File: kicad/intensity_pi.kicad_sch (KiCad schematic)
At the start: 68 parts, among them J1 Input A, J2 Input B / Setpoint, J3 Monitor, J4 Output, J7 select 1, SW1 SW_SPDT, SW2 SW_SPDT, SW3 SW_SPDT, SW5 EG6100-ND, U1 LM4040DBZ-5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

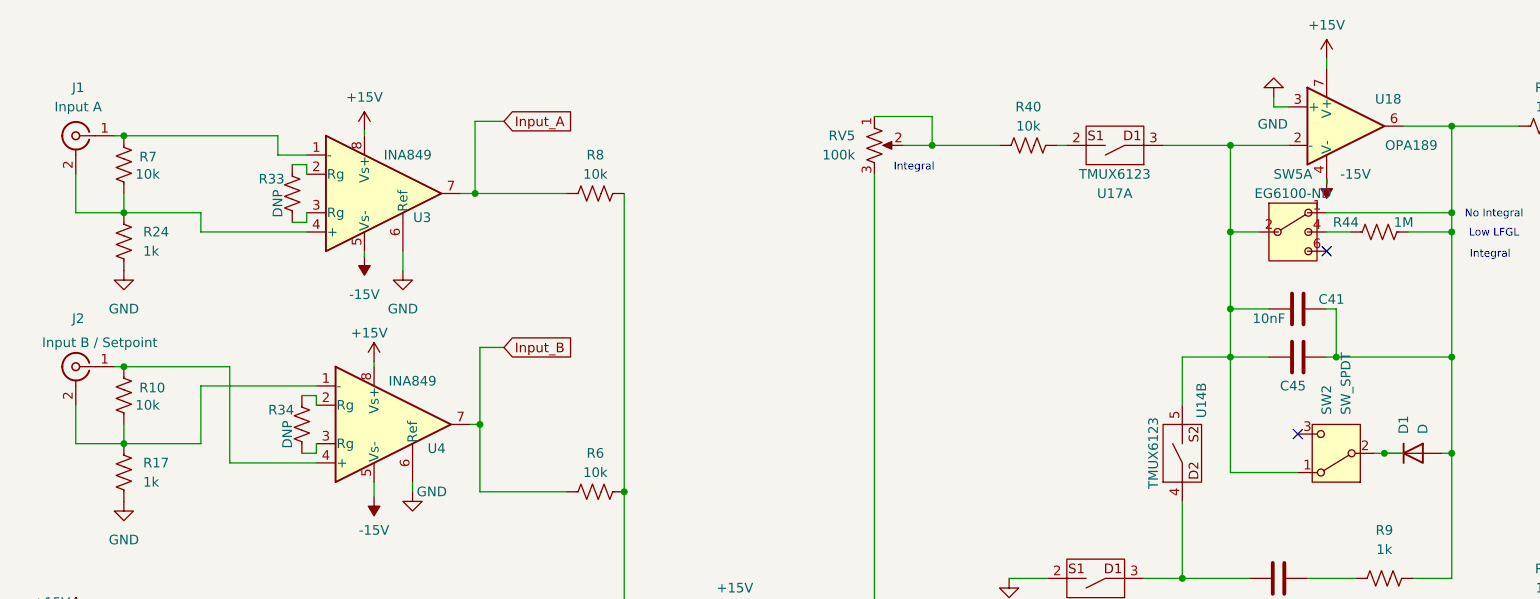
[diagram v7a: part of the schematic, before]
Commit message: V1.1, Fixedincorrect footprints for Green/Red LED, Diodes, Mosfets, Flipped Input A/B Polarity, Potentiometer labels, Incorrect part nos for V regulators. No functionality changes
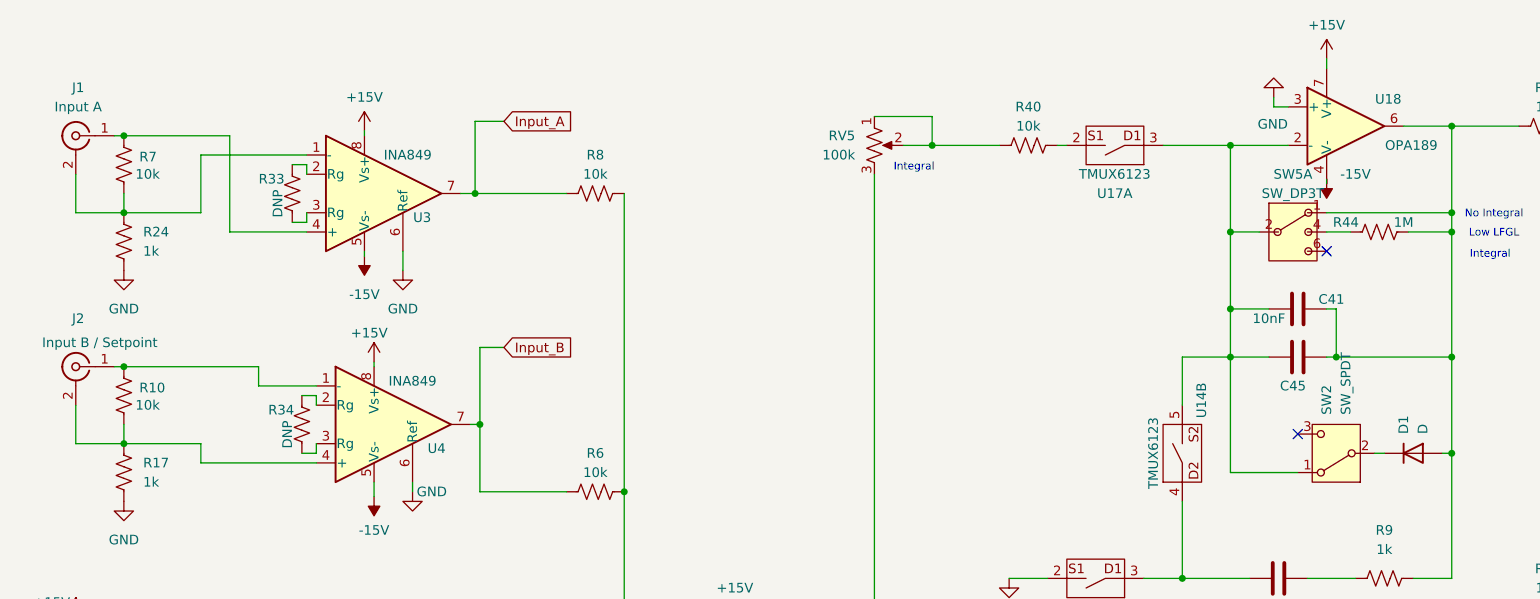
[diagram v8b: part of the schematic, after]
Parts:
- SW5: value EG6100-ND -> SW_DP3T
- U3, U4: PARTNO INA849DR‎ -> INA849DR
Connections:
- net at J1.1 (In), R7.2: now also U3.4 (+); no longer U3.1 (-)
- net at J1.2 (Ext), R24.2, R7.1: now also U3.1 (-); no longer U3.4 (+)
- net at C41.1, C45.2, R19.1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: now also D1.3 (A); no longer D1.2 (A)
- net at J2.2 (Ext), R10.1, R17.2: now also U4.4 (+); no longer U4.1 (-)
- net at J2.1 (In), R10.2: now also U4.1 (-); no longer U4.4 (+)
- net at SW3.2 (B): now also D2.3 (A); no longer D2.2 (A)
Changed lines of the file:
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@@
 	)
 	(junction
-		(at 191.77 71.12)
+		(at 25.4 29.21)
 		(diameter 0)
 		(color 0 0 0 0)
@@
 	)
 	(junction
-		(at 25.4 29.21)
-		(diameter 0)
-		(color 0 0 0 0)
-	)
-	(junction
 		(at 200.66 58.42)
 		(diameter 0)
@@
 	(wire
 		(pts
+			(xy 25.4 29.21) (xy 39.37 29.21)
+		)
+		(stroke
+			(width 0)
+			(type default)
+		)
+	)
+	(wire
+		(pts
 			(xy 219.71 91.44) (xy 219.71 104.14)
 		)
@@
 	(wire
 		(pts
+			(xy 35.56 39.37) (xy 35.56 31.75)
+		)
+		(stroke
+			(width 0)
+			(type default)
+		)
+	)
+	(wire
+		(pts
 			(xy 72.39 144.78) (xy 72.39 135.89)
 		)
@@
 	(wire
 		(pts
-			(xy 191.77 71.12) (xy 194.31 71.12)
-		)
-		(stroke
-			(width 0)
-			(type default)
-		)
-	)
-	(wire
-		(pts
 			(xy 59.69 173.99) (xy 59.69 177.8)
 		)
@@
 	(wire
 		(pts
-			(xy 158.75 181.61) (xy 157.48 181.61)
+			(xy 43.18 59.69) (xy 43.18 62.23)
 		)
 		(stroke
@@
 	(wire
 		(pts
-			(xy 165.1 58.42) (xy 171.45 58.42)
+			(xy 158.75 181.61) (xy 157.48 181.61)
 		)
 		(stroke
@@
 	(wire
 		(pts
-			(xy 106.045 93.345) (xy 106.045 93.98)
+			(xy 165.1 58.42) (xy 171.45 58.42)
 		)
 		(stroke
@@
 	(wire
 		(pts
-			(xy 34.29 116.84) (xy 37.465 116.84)
+			(xy 106.045 93.345) (xy 106.045 93.98)
 		)
 		(stroke
@@
 	(wire
 		(pts
-			(xy 189.23 135.89) (xy 203.2 135.89)
+			(xy 34.29 116.84) (xy 37.465 116.84)
 		)
 		(stroke
@@
 	(wire
 		(pts
-			(xy 35.56 41.91) (xy 49.53 41.91)
+			(xy 189.23 135.89) (xy 203.2 135.89)
 		)
 		(stroke
@@
 	(wire
 		(pts
-			(xy 35.56 41.91) (xy 35.56 39.37)
-		)
-		(stroke
-			(width 0)
-			(type default)
-		)
-	)
-	(wire
-		(pts
 			(xy 147.32 128.27) (xy 147.32 130.81)
 		)
@@
 	(wire
 		(pts
-			(xy 118.11 121.92) (xy 118.11 123.19)
+			(xy 39.37 29.21) (xy 39.37 41.91)
 		)
 		(stroke
@@
 	(wire
 		(pts
-			(xy 52.07 135.89) (xy 52.07 138.43)
+			(xy 118.11 121.92) (xy 118.11 123.19)
 		)
 		(stroke
@@
 	(wire
 		(pts
-			(xy 184.15 58.42) (xy 185.42 58.42)
+			(xy 52.07 135.89) (xy 52.07 138.43)
 		)
 		(stroke
@@
 	(wire
 		(pts
-			(xy 45.72 29.21) (xy 45.72 31.75)
+			(xy 184.15 58.42) (xy 185.42 58.42)
 		)
 		(stroke
@@
 	(wire
 		(pts
+			(xy 35.56 31.75) (xy 49.53 31.75)
+		)
+		(stroke
+			(width 0)
+			(type default)
+		)
+	)
+	(wire
+		(pts
 			(xy 72.39 119.38) (xy 72.39 135.89)
 		)
@@
 	(wire
 		(pts
-			(xy 35.56 62.23) (xy 50.8 62.23)
-		)
-		(stroke
-			(width 0)
-			(type default)
-		)
-	)
-	(wire
-		(pts
 			(xy 22.86 130.81) (xy 19.05 130.81)
 		)
@@
 	(wire
 		(pts
-			(xy 39.37 72.39) (xy 50.8 72.39)
-		)
-		(stroke
-			(width 0)
-			(type default)
-		)
-	)
-	(wire
-		(pts
 			(xy 203.2 151.765) (xy 203.2 160.02)
 		)
@@
 	(wire
 		(pts
-			(xy 116.84 196.85) (xy 116.84 184.15)
+			(xy 35.56 69.85) (xy 35.56 72.39)
 		)
 		(stroke
@@
 	(wire
 		(pts
-			(xy 25.4 29.21) (xy 45.72 29.21)
+			(xy 116.84 196.85) (xy 116.84 184.15)
 		)
 		(stroke
@@
 	(wire
 		(pts
-			(xy 132.08 26.67) (xy 132.08 30.48)
+			(xy 39.37 41.91) (xy 49.53 41.91)
 		)
 		(stroke
@@
 	(wire
 		(pts
-			(xy 219.71 114.3) (xy 234.315 114.3)
+			(xy 132.08 26.67) (xy 132.08 30.48)
 		)
 		(stroke
@@
 	(wire
 		(pts
-			(xy 35.56 69.85) (xy 35.56 62.23)
+			(xy 219.71 114.3) (xy 234.315 114.3)
 		)
 		(stroke
@@
 	(wire
 		(pts
-			(xy 45.72 31.75) (xy 49.53 31.75)
-		)
-		(stroke
-			(width 0)
-			(type default)
-		)
-	)
-	(wire
-		(pts
 			(xy 241.3 80.01) (xy 243.84 80.01)
 		)
@@
 	(wire
 		(pts
+			(xy 43.18 62.23) (xy 50.8 62.23)
+		)
+		(stroke
+			(width 0)
+			(type default)
+		)
+	)
+	(wire
+		(pts
 			(xy 254 132.08) (xy 262.89 132.08)
 		)
@@
 	(wire
 		(pts
+			(xy 35.56 72.39) (xy 50.8 72.39)
+		)
+		(stroke
+			(width 0)
+			(type default)
+		)
+	)
+	(wire
+		(pts
 			(xy 142.24 87.63) (xy 147.32 87.63)
 		)
@@
 	(wire
 		(pts
-			(xy 25.4 59.69) (xy 39.37 59.69)
+			(xy 25.4 59.69) (xy 43.18 59.69)
 		)
 		(stroke
@@
 	(wire
 		(pts
-			(xy 39.37 59.69) (xy 39.37 72.39)
-		)
-		(stroke
-			(width 0)
-			(type default)
-		)
-	)
-	(wire
-		(pts
 			(xy 100.965 104.14) (xy 91.44 104.14)
 		)
@@
 			)
 		)
-		(property "PARTNO" "INA849DR‎ "
+		(property "PARTNO" "INA849DR"
 			(at 59.69 36.83 0)
 			(effects
@@
 	)
 	(symbol
+		(lib_name "D_1")
 		(lib_id "Device:D")
 		(at 195.58 71.12 0)
@@
 		(pin "1"
 		)
-		(pin "2"
+		(pin "3"
 		)
 		(instances
@@
 			)
 		)
-		(property "Value" "EG6100-ND"
+		(property "Value" "SW_DP3T"
 			(at 179.705 36.83 0)
 			(effects
@@
 		(pin "1"
 		)
-		(pin "2"
+		(pin "3"
 		)
 		(instances
@@
 			)
 		)
-		(property "PARTNO" "INA849DR‎ "
+		(property "PARTNO" "INA849DR"
 			(at 60.96 67.31 0)
 			(effects
